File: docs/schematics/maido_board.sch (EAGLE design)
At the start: 40 parts

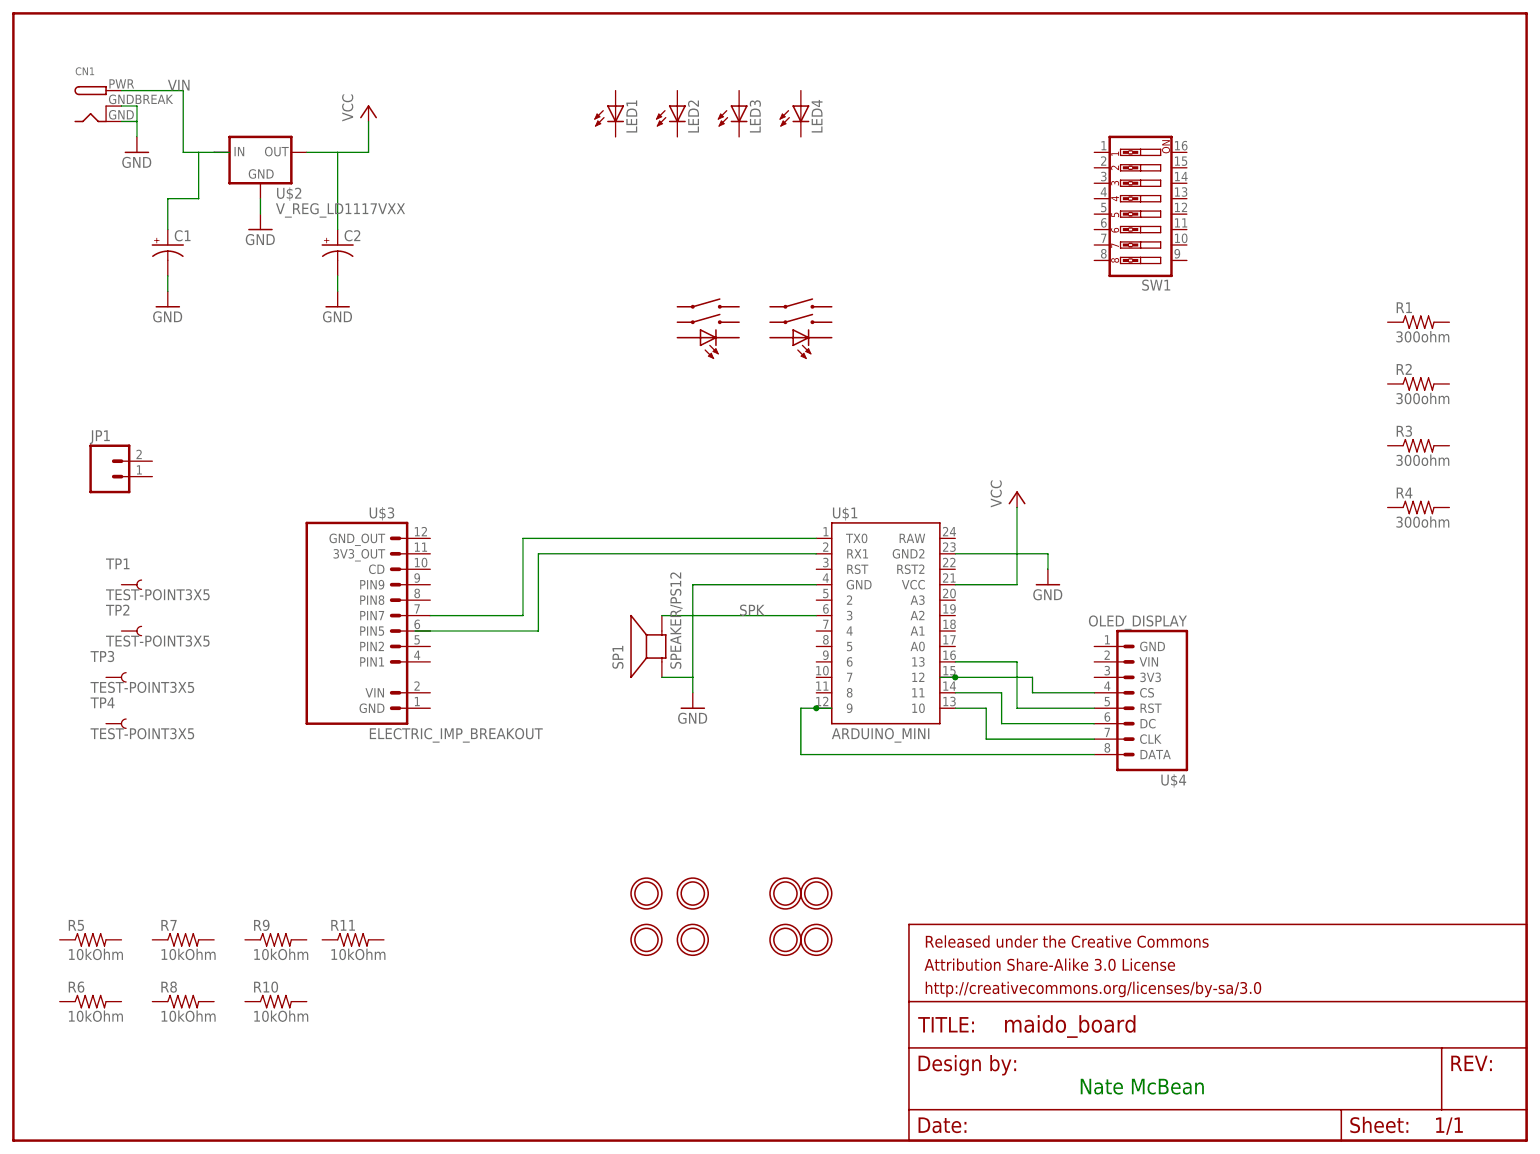
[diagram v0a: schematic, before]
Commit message: Initial Layout
Schematic completely wired. Have initial placement (no routing)
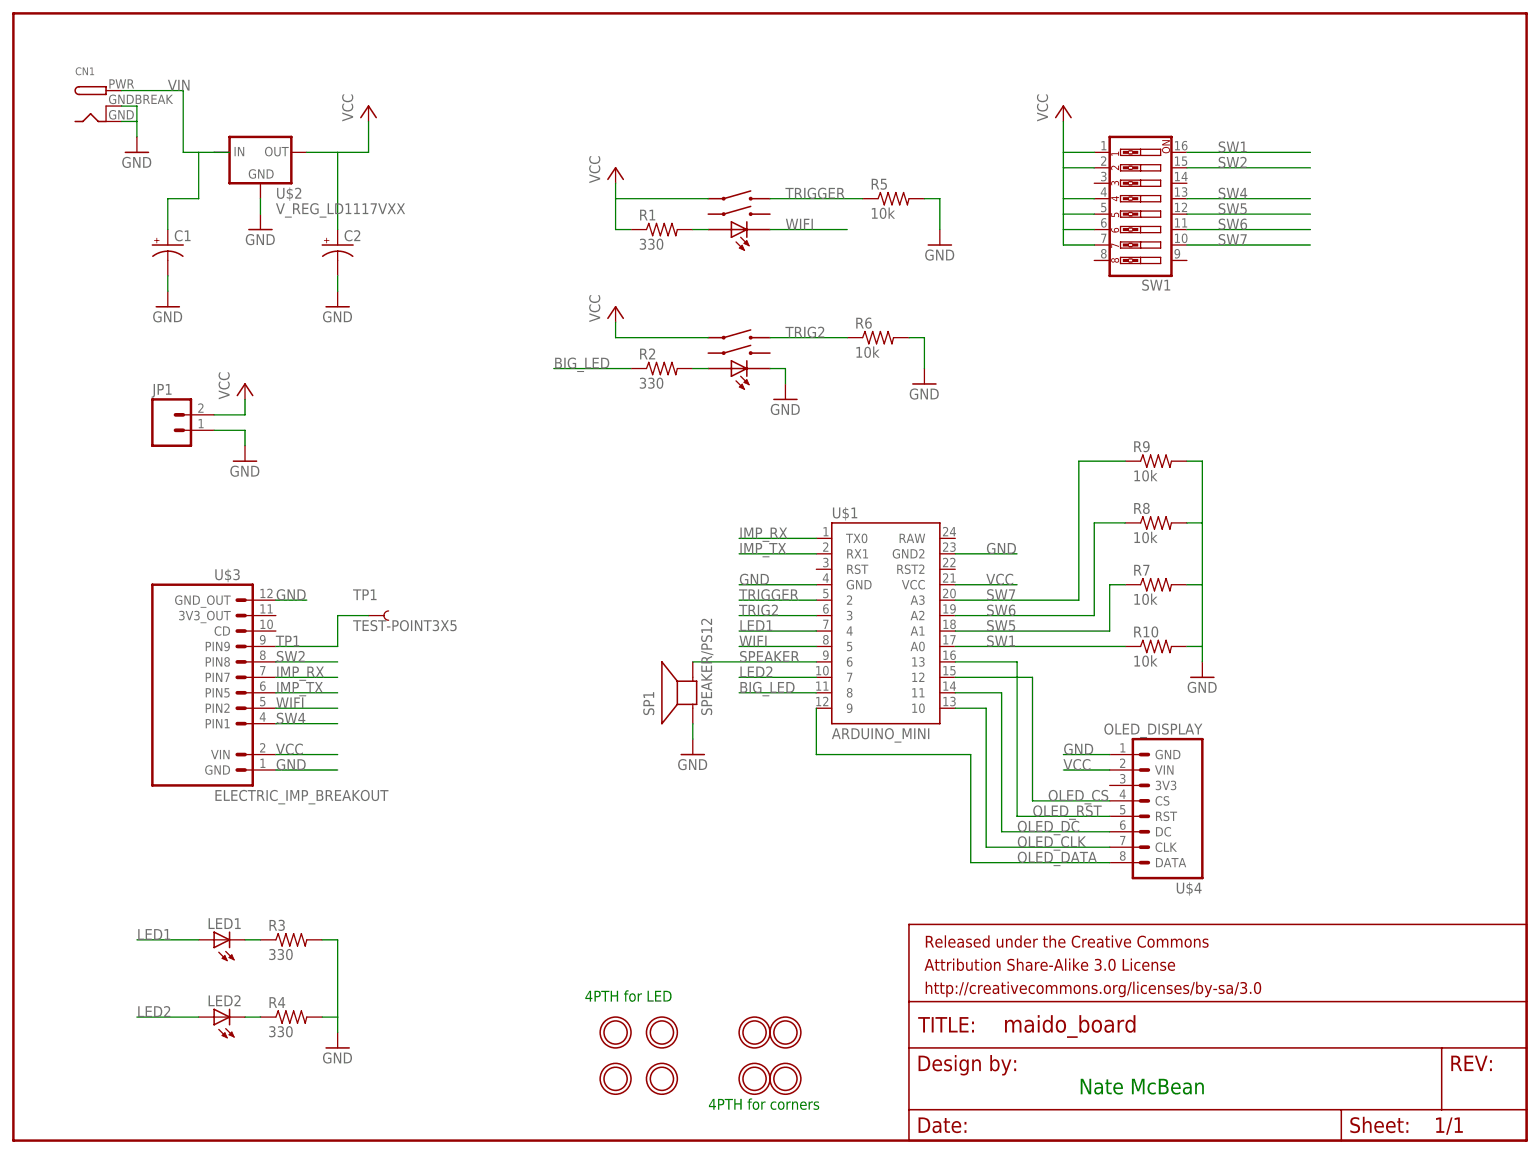
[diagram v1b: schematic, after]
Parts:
- removed LED3, LED4: (no value), SparkFun-LED:LED5MM
- removed R11: 10kOhm, adafruit:R-US_R0805
- removed TP2, TP3, TP4: TEST-POINT3X5, SparkFun-Passives:TEST-POINT3X5
- R1, R2, R3, R4: value 300ohm -> 330
- R10, R5, R6, R7, R8, R9: value 10kOhm -> 10k
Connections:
- net N$1 renamed OLED_DATA
- net N$2 renamed OLED_CLK
- net N$3 renamed OLED_DC
- net N$4 renamed OLED_CS
- net N$5 renamed OLED_RST
- net N$7 renamed IMP_RX
- removed net N$6: U$1.RX1
- removed net SPK: SP1.-, U$1.3
- new net BIG_LED: R2.1, U$1.8
- new net IMP_TX: U$1.RX1, U$3.PIN5
- new net LED1: LED1.A, U$1.4
- new net LED2: LED2.A, U$1.7
- new net N$1: LSW1.LEDA, R1.2
- new net N$2: LSW2.LEDA, R2.2
- new net N$3: LED1.C, R3.1
- new net N$4: LED2.C, R4.1
- new net SPEAKER: SP1.-, U$1.6
- new net SW1: R10.1, SW1.16, U$1.A0
- new net SW2: SW1.15, U$3.PIN8
- new net SW4: SW1.13, U$3.PIN1
- new net SW5: R7.1, SW1.12, U$1.A1
- new net SW6: R8.1, SW1.11, U$1.A2
- new net SW7: R9.1, SW1.10, U$1.A3
- new net TP1: TP1.1, U$3.PIN9
- new net TRIG2: LSW2.SWA2, R6.1, U$1.3
- new net TRIGGER: LSW1.SWA2, R5.1, U$1.2
- new net WIFI: LSW1.LEDC, U$1.5, U$3.PIN2
- net GND: now also JP1.1, LSW2.LEDC, R10.2, R3.2, R4.2, R5.2, R6.2, R7.2, R8.2, R9.2, U$3.GND, U$3.GND_OUT, U$4.GND
- net VCC: now also JP1.2, LSW1.SWA1, LSW2.SWA1, R1.1, SW1.1, SW1.2, SW1.4, SW1.5, SW1.6, SW1.7, U$3.VIN, U$4.VIN
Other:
- note added: "4PTH for LED"
- note added: "4PTH for corners"
- moved on the sheet: JP1, LED1, LED2, R1, R10, R2, R3, R4, R5, R6, R7, R8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

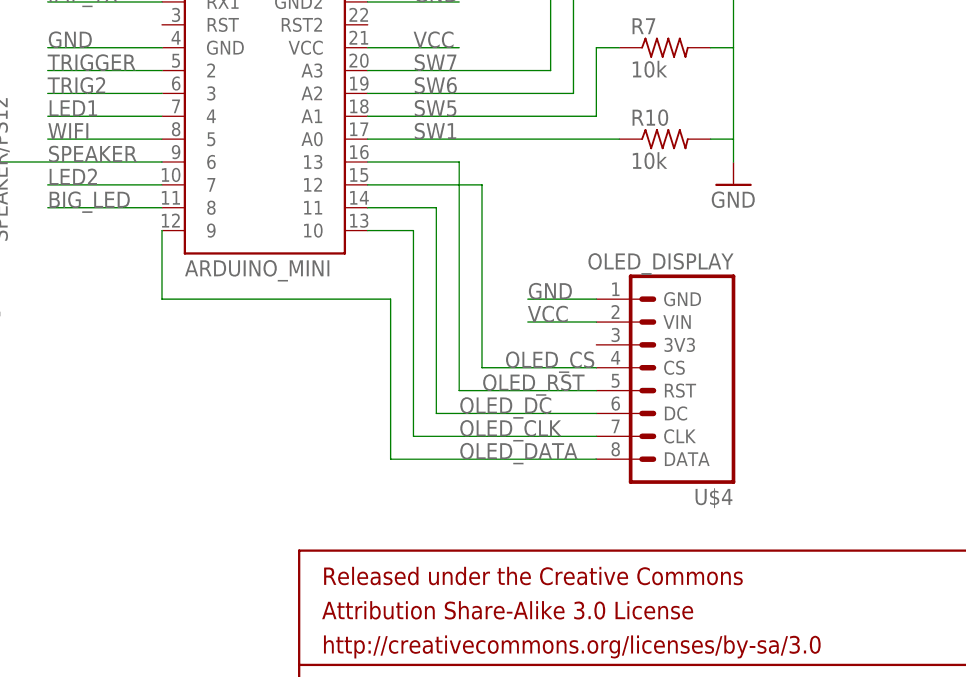
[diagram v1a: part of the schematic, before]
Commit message: Fixed pinout on OLED
Oops! That would have been a horrible mistake. I also messed around with
routing some.
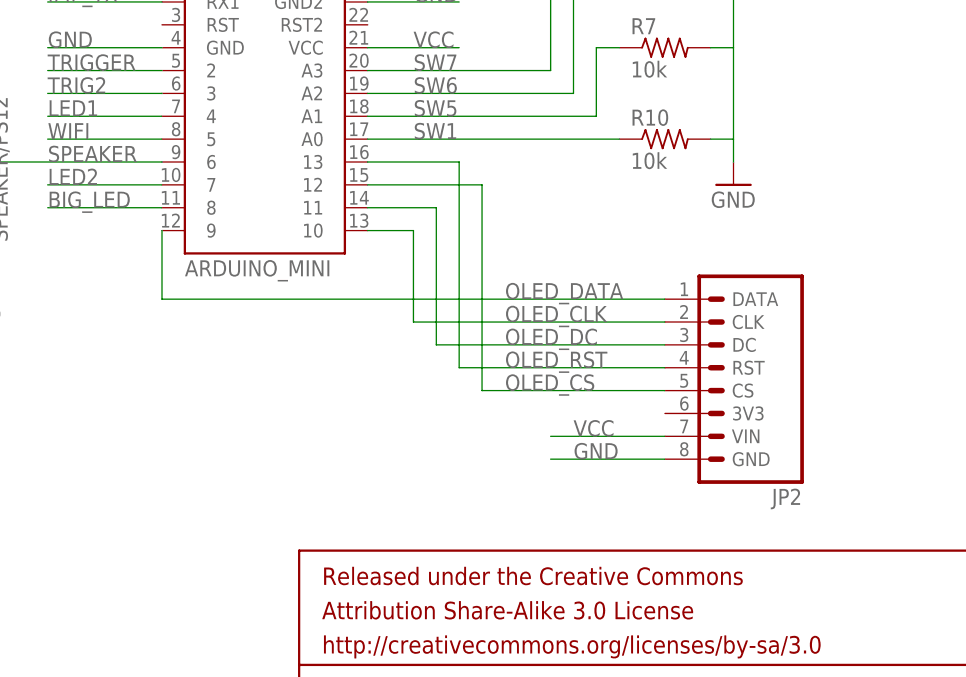
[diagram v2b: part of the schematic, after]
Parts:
- removed U$4: OLED_DISPLAY, nate_parts:OLED128X641X08
- added JP2: (no value), nate_parts:OLED128X641X08
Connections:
- net GND: now also JP2.GND; no longer U$4.GND
- net OLED_CLK: now also JP2.CLK; no longer U$4.CLK
- net OLED_CS: now also JP2.CS; no longer U$4.CS
- net OLED_DATA: now also JP2.DATA; no longer U$4.DATA
- net OLED_DC: now also JP2.DC; no longer U$4.DC
- net OLED_RST: now also JP2.RST; no longer U$4.RST
- net VCC: now also JP2.VIN; no longer U$4.VIN
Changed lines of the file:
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@@
 <part name="GND6" library="supply1" deviceset="GND" device=""/>
 <part name="U$3" library="nate_parts" deviceset="ELECTRIC_IMP_BREAKOUT" device=""/>
-<part name="U$4" library="nate_parts" deviceset="OLED128X64" device="1X08" value="OLED_DISPLAY"/>
 <part name="LSW1" library="SparkFun-LED_Tactile_Button" deviceset="LED_TACTILE_BUTTON" device=""/>
 <part name="R2" library="adafruit" deviceset="R-US_" device="R0805" value="330"/>
@@
 <part name="GND10" library="supply1" deviceset="GND" device=""/>
 <part name="GND11" library="supply1" deviceset="GND" device=""/>
+<part name="JP2" library="nate_parts" deviceset="OLED128X64" device="1X08"/>
 </parts>
 <sheets>
@@
 <instance part="GND6" gate="1" x="109.22" y="53.34"/>
 <instance part="U$3" gate="G$1" x="30.48" y="68.58"/>
-<instance part="U$4" gate="G$1" x="182.88" y="45.72" rot="R180"/>
 <instance part="LSW1" gate="LSW" x="116.84" y="142.24"/>
 <instance part="R2" gate="G$1" x="104.14" y="116.84"/>
@@
 <instance part="GND10" gate="1" x="124.46" y="111.76"/>
 <instance part="GND11" gate="1" x="50.8" y="5.08"/>
+<instance part="JP2" gate="G$1" x="190.5" y="45.72" rot="R180"/>
 </instances>
 <busses>
@@
 </segment>
 <segment>
-<pinref part="U$4" gate="G$1" pin="VIN"/>
-<wire x1="177.8" y1="50.8" x2="170.18" y2="50.8" width="0.2032" layer="91"/>
-<label x="170.18" y="50.8" size="1.778" layer="95"/>
+<wire x1="185.42" y1="38.1" x2="172.72" y2="38.1" width="0.2032" layer="91"/>
+<label x="175.26" y="38.1" size="1.778" layer="95"/>
+<pinref part="JP2" gate="G$1" pin="VIN"/>
 </segment>
 </net>
@@
 </segment>
 <segment>
-<pinref part="U$4" gate="G$1" pin="GND"/>
-<wire x1="177.8" y1="53.34" x2="170.18" y2="53.34" width="0.2032" layer="91"/>
-<label x="170.18" y="53.34" size="1.778" layer="95"/>
-</segment>
-<segment>
 <pinref part="U$1" gate="G$1" pin="GND2"/>
 <wire x1="152.4" y1="86.36" x2="162.56" y2="86.36" width="0.2032" layer="91"/>
@@
 <wire x1="50.8" y1="22.86" x2="50.8" y2="10.16" width="0.2032" layer="91"/>
 </segment>
+<segment>
+<wire x1="172.72" y1="35.56" x2="185.42" y2="35.56" width="0.2032" layer="91"/>
+<label x="175.26" y="35.56" size="1.778" layer="95"/>
+<pinref part="JP2" gate="G$1" pin="GND"/>
+</segment>
 </net>
 <net name="OLED_CLK" class="0">
@@
 <pinref part="U$1" gate="G$1" pin="10"/>
 <wire x1="152.4" y1="60.96" x2="157.48" y2="60.96" width="0.2032" layer="91"/>
-<wire x1="157.48" y1="60.96" x2="157.48" y2="38.1" width="0.2032" layer="91"/>
-<pinref part="U$4" gate="G$1" pin="CLK"/>
-<wire x1="157.48" y1="38.1" x2="177.8" y2="38.1" width="0.2032" layer="91"/>
-<label x="162.56" y="38.1" size="1.778" layer="95"/>
+<wire x1="157.48" y1="60.96" x2="157.48" y2="50.8" width="0.2032" layer="91"/>
+<wire x1="157.48" y1="50.8" x2="185.42" y2="50.8" width="0.2032" layer="91"/>
+<label x="167.64" y="50.8" size="1.778" layer="95"/>
+<pinref part="JP2" gate="G$1" pin="CLK"/>
 </segment>
 </net>
@@
 <pinref part="U$1" gate="G$1" pin="11"/>
 <wire x1="152.4" y1="63.5" x2="160.02" y2="63.5" width="0.2032" layer="91"/>
-<wire x1="160.02" y1="63.5" x2="160.02" y2="40.64" width="0.2032" layer="91"/>
-<pinref part="U$4" gate="G$1" pin="DC"/>
-<wire x1="160.02" y1="40.64" x2="177.8" y2="40.64" width="0.2032" layer="91"/>
-<label x="162.56" y="40.64" size="1.778" layer="95"/>
+<wire x1="160.02" y1="63.5" x2="160.02" y2="48.26" width="0.2032" layer="91"/>
+<wire x1="160.02" y1="48.26" x2="185.42" y2="48.26" width="0.2032" layer="91"/>
+<label x="167.64" y="48.26" size="1.778" layer="95"/>
+<pinref part="JP2" gate="G$1" pin="DC"/>
 </segment>
 </net>
@@
 <pinref part="U$1" gate="G$1" pin="13"/>
 <wire x1="152.4" y1="68.58" x2="162.56" y2="68.58" width="0.2032" layer="91"/>
-<wire x1="162.56" y1="68.58" x2="162.56" y2="43.18" width="0.2032" layer="91"/>
-<pinref part="U$4" gate="G$1" pin="RST"/>
-<wire x1="162.56" y1="43.18" x2="177.8" y2="43.18" width="0.2032" layer="91"/>
-<label x="165.1" y="43.18" size="1.778" layer="95"/>
+<wire x1="162.56" y1="68.58" x2="162.56" y2="45.72" width="0.2032" layer="91"/>
+<wire x1="162.56" y1="45.72" x2="185.42" y2="45.72" width="0.2032" layer="91"/>
+<label x="167.64" y="45.72" size="1.778" layer="95"/>
+<pinref part="JP2" gate="G$1" pin="RST"/>
 </segment>
 </net>
@@
 <pinref part="U$1" gate="G$1" pin="9"/>
 <wire x1="129.54" y1="60.96" x2="129.54" y2="53.34" width="0.2032" layer="91"/>
-<wire x1="129.54" y1="53.34" x2="154.94" y2="53.34" width="0.2032" layer="91"/>
-<wire x1="154.94" y1="53.34" x2="154.94" y2="35.56" width="0.2032" layer="91"/>
-<pinref part="U$4" gate="G$1" pin="DATA"/>
-<wire x1="154.94" y1="35.56" x2="177.8" y2="35.56" width="0.2032" layer="91"/>
-<label x="162.56" y="35.56" size="1.778" layer="95"/>
+<wire x1="129.54" y1="53.34" x2="185.42" y2="53.34" width="0.2032" layer="91"/>
+<label x="167.64" y="53.34" size="1.778" layer="95"/>
+<pinref part="JP2" gate="G$1" pin="DATA"/>
 </segment>
 </net>
 <net name="OLED_CS" class="0">
 <segment>
-<pinref part="U$4" gate="G$1" pin="CS"/>
-<wire x1="177.8" y1="45.72" x2="165.1" y2="45.72" width="0.2032" layer="91"/>
-<wire x1="165.1" y1="45.72" x2="165.1" y2="66.04" width="0.2032" layer="91"/>
+<wire x1="165.1" y1="43.18" x2="165.1" y2="66.04" width="0.2032" layer="91"/>
 <pinref part="U$1" gate="G$1" pin="12"/>
 <wire x1="165.1" y1="66.04" x2="152.4" y2="66.04" width="0.2032" layer="91"/>
-<label x="167.64" y="45.72" size="1.778" layer="95"/>
-</segment>
-</net>
+<wire x1="165.1" y1="43.18" x2="185.42" y2="43.18" width="0.2032" layer="91"/>
+<label x="167.64" y="43.18" size="1.778" layer="95"/>
+<pinref part="JP2" gate="G$1" pin="CS"/>
+</segment>
+</net>

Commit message: Layout Work
More work on the layout. I pretty carefully managed power to from the DC
header to the VREG to the Imp (by FAR the biggest power consumer on the
board). I also rearranged some parts to try to optimize placement. Next
up- auto route.
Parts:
- U$2: value V_REG_LD1117VXX -> VREG
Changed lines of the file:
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@@
 <part name="U$1" library="SparkFun-Boards" deviceset="ARDUINO_MINI" device=""/>
 <part name="FRAME1" library="SparkFun-Aesthetics" deviceset="FRAME-LETTER" device=""/>
-<part name="U$2" library="SparkFun-PowerIC" deviceset="V_REG_LD1117VXX" device=""/>
+<part name="U$2" library="SparkFun-PowerIC" deviceset="V_REG_LD1117VXX" device="" value="VREG"/>
 <part name="C1" library="SparkFun-Passives" deviceset="CAP_POL" device="PTH2"/>
 <part name="C2" library="SparkFun-Passives" deviceset="CAP_POL" device="PTH2"/>

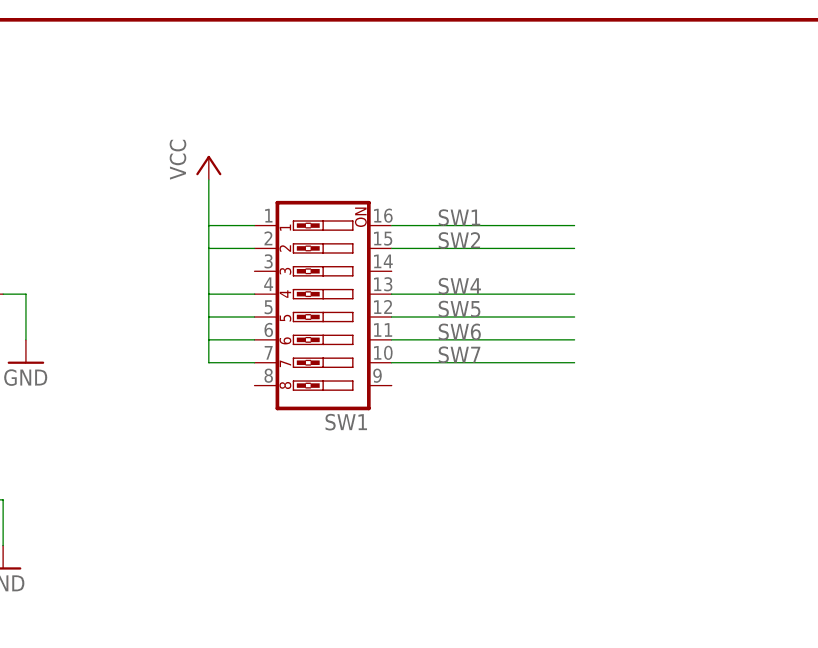
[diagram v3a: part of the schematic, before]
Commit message: Final Built Board
Final built board schematic + layout (received board already, tested,
works). Added IO pins to the arduino code, works.
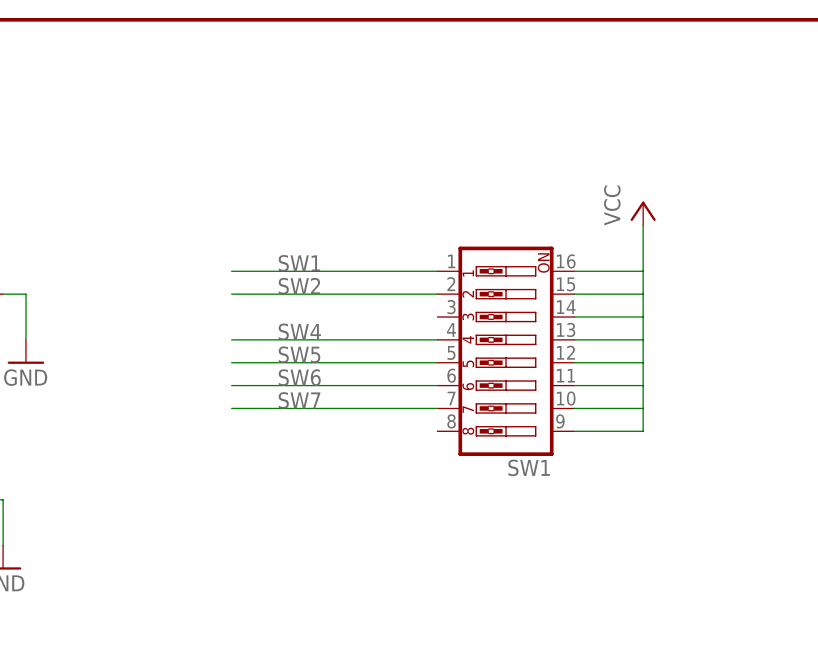
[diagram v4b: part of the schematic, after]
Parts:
- renumbered LSW1 to SEND, LSW2 to ACK
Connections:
- net SW1: now also SW1.1; no longer SW1.16
- net SW2: now also SW1.2; no longer SW1.15
- net SW4: now also SW1.4; no longer SW1.13
- net SW5: now also SW1.5; no longer SW1.12
- net SW6: now also SW1.6; no longer SW1.11
- net SW7: now also SW1.7; no longer SW1.10
- net VCC: now also SW1.10, SW1.11, SW1.12, SW1.13, SW1.14, SW1.15, SW1.16, SW1.9; no longer SW1.1, SW1.2, SW1.4, SW1.5, SW1.6, SW1.7
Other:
- moved on the sheet: SW1
